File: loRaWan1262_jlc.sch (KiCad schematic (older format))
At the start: 6 parts

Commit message: Add digikey pn's to schematic, update BOM
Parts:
- H1, H2, H3, H4: Digikey (none) -> DNP; LCSC (none) -> DNP
- R18, R19: Digikey (none) -> 311-4.7KJRCT-ND
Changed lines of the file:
@@
 F 2 "MountingHole:MountingHole_2.7mm_M2.5" H 8750 5600 50  0001 C CNN
 F 3 "~" H 8750 5600 50  0001 C CNN
+F 4 "DNP" H 8750 5600 50  0001 C CNN "LCSC"
+F 5 "DNP" H 8750 5600 50  0001 C CNN "Digikey"
 	1    8750 5600
 	1    0    0    -1
@@
 F 2 "MountingHole:MountingHole_2.7mm_M2.5" H 9050 5600 50  0001 C CNN
 F 3 "~" H 9050 5600 50  0001 C CNN
+F 4 "DNP" H 9050 5600 50  0001 C CNN "LCSC"
+F 5 "DNP" H 9050 5600 50  0001 C CNN "Digikey"
 	1    9050 5600
 	1    0    0    -1
@@
 F 2 "MountingHole:MountingHole_2.7mm_M2.5_Pad" H 9350 5650 50  0001 C CNN
 F 3 "~" H 9350 5650 50  0001 C CNN
+F 4 "DNP" H 9350 5650 50  0001 C CNN "LCSC"
+F 5 "DNP" H 9350 5650 50  0001 C CNN "Digikey"
 	1    9350 5650
 	1    0    0    -1
@@
 F 2 "MountingHole:MountingHole_2.7mm_M2.5_Pad" H 9650 5650 50  0001 C CNN
 F 3 "~" H 9650 5650 50  0001 C CNN
+F 4 "DNP" H 9650 5650 50  0001 C CNN "LCSC"
+F 5 "DNP" H 9650 5650 50  0001 C CNN "Digikey"
 	1    9650 5650
 	1    0    0    -1
@@
 F 3 "~" H 5600 2550 50  0001 C CNN
 F 4 "C25900" H 5600 2550 50  0001 C CNN "LCSC"
+F 5 "311-4.7KJRCT-ND" H 5600 2550 50  0001 C CNN "Digikey"
 	1    5600 2550
 	1    0    0    -1
@@
 F 3 "~" H 5900 2550 50  0001 C CNN
 F 4 "C25900" H 5900 2550 50  0001 C CNN "LCSC"
+F 5 "311-4.7KJRCT-ND" H 5900 2550 50  0001 C CNN "Digikey"
 	1    5900 2550
 	1    0    0    -1
@@
 	5900 2300 5900 2400
 Connection ~ 5750 2300
-Wire Wire Line
-	4900 5500 6950 5500
-Wire Wire Line
-	4900 5300 6950 5300
-Wire Bus Line
-	4800 3650 4800 5850
-Wire Bus Line
-	5000 3750 5000 5850
-Wire Bus Line
-	4800 1250 4800 3650
 $Comp
-L Graphic:Logo_Open_Hardware_Small #LOGO?
+L Graphic:Logo_Open_Hardware_Small #LOGO1
 U 1 1 5DD2C4B6
 P 10800 6850
-F 0 "#LOGO?" H 10800 7125 50  0001 C CNN
+F 0 "#LOGO1" H 10800 7125 50  0001 C CNN
 F 1 "Logo_Open_Hardware_Small" H 10800 6625 50  0001 C CNN
 F 2 "" H 10800 6850 50  0001 C CNN
@@
 $EndComp
 $Comp
-L Graphic:SYM_Radio_Waves_Large #SYM?
+L Graphic:SYM_Radio_Waves_Large #SYM1
 U 1 1 5DD2D71A
 P 10250 6800
-F 0 "#SYM?" H 10250 7000 50  0001 C CNN
+F 0 "#SYM1" H 10250 7000 50  0001 C CNN
 F 1 "SYM_Radio_Waves_Large" H 10250 6550 50  0001 C CNN
 F 2 "" H 10250 6600 50  0001 C CNN
@@
 EndData
 $EndBitmap
+Wire Wire Line
+	4900 5500 6950 5500
+Wire Wire Line
+	4900 5300 6950 5300
+Wire Bus Line
+	4800 3650 4800 5850
+Wire Bus Line
+	5000 3750 5000 5850
+Wire Bus Line
+	4800 1250 4800 3650
 $EndSCHEMATC

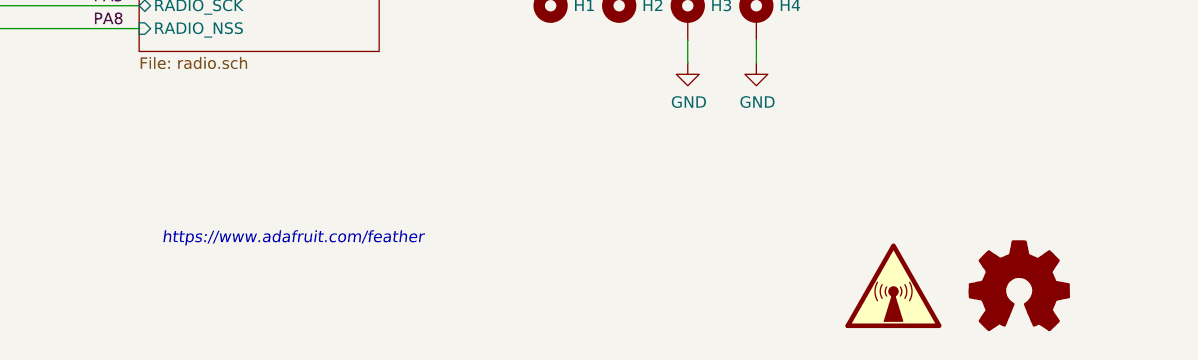
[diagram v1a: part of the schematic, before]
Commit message: PCB REV C0 * Make U8 footprint capable of crypto and fram device * Minor updates to schematic * Minor updates to doc prints * Update bot silk to REV C0
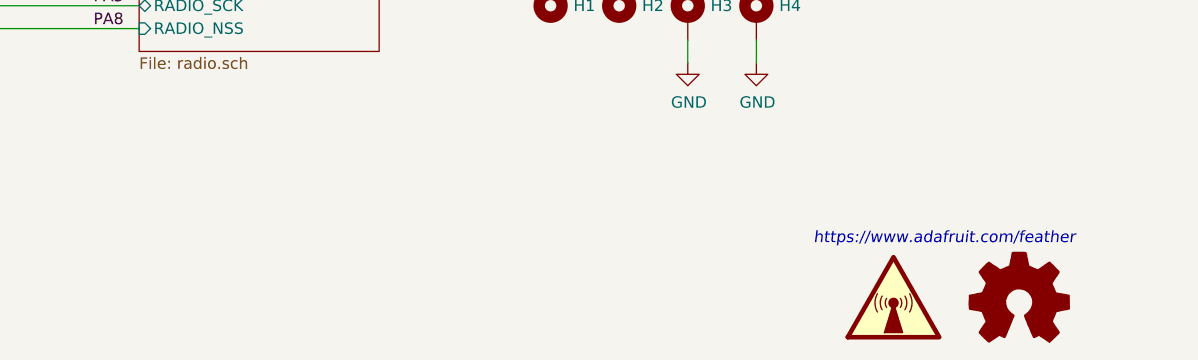
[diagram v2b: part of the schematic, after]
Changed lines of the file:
@@
 L Graphic:Logo_Open_Hardware_Small #LOGO1
 U 1 1 5DD2C4B6
-P 10800 6850
-F 0 "#LOGO1" H 10800 7125 50  0001 C CNN
-F 1 "Logo_Open_Hardware_Small" H 10800 6625 50  0001 C CNN
-F 2 "" H 10800 6850 50  0001 C CNN
-F 3 "~" H 10800 6850 50  0001 C CNN
-	1    10800 6850
+P 10800 6900
+F 0 "#LOGO1" H 10800 7175 50  0001 C CNN
+F 1 "Logo_Open_Hardware_Small" H 10800 6675 50  0001 C CNN
+F 2 "" H 10800 6900 50  0001 C CNN
+F 3 "~" H 10800 6900 50  0001 C CNN
+	1    10800 6900
 	1    0    0    -1
 $EndComp
@@
 L Graphic:SYM_Radio_Waves_Large #SYM1
 U 1 1 5DD2D71A
-P 10250 6800
-F 0 "#SYM1" H 10250 7000 50  0001 C CNN
-F 1 "SYM_Radio_Waves_Large" H 10250 6550 50  0001 C CNN
-F 2 "" H 10250 6600 50  0001 C CNN
-F 3 "~" H 10280 6600 50  0001 C CNN
-	1    10250 6800
+P 10250 6850
+F 0 "#SYM1" H 10250 7050 50  0001 C CNN
+F 1 "SYM_Radio_Waves_Large" H 10250 6600 50  0001 C CNN
+F 2 "" H 10250 6650 50  0001 C CNN
+F 3 "~" H 10280 6650 50  0001 C CNN
+	1    10250 6850
 	1    0    0    -1
 $EndComp
@@
 EndData
 $EndBitmap
-Text Notes 7050 6650 0    50   Italic 0
+Text Notes 9900 6650 0    50   Italic 0
 https://www.adafruit.com/feather
 $Bitmap
